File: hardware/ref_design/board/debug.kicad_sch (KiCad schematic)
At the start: 7 parts, among them J5 SWD, J6 UART, J7 DEBUG PADS, SW18 BOOTSEL, SW19 RESET

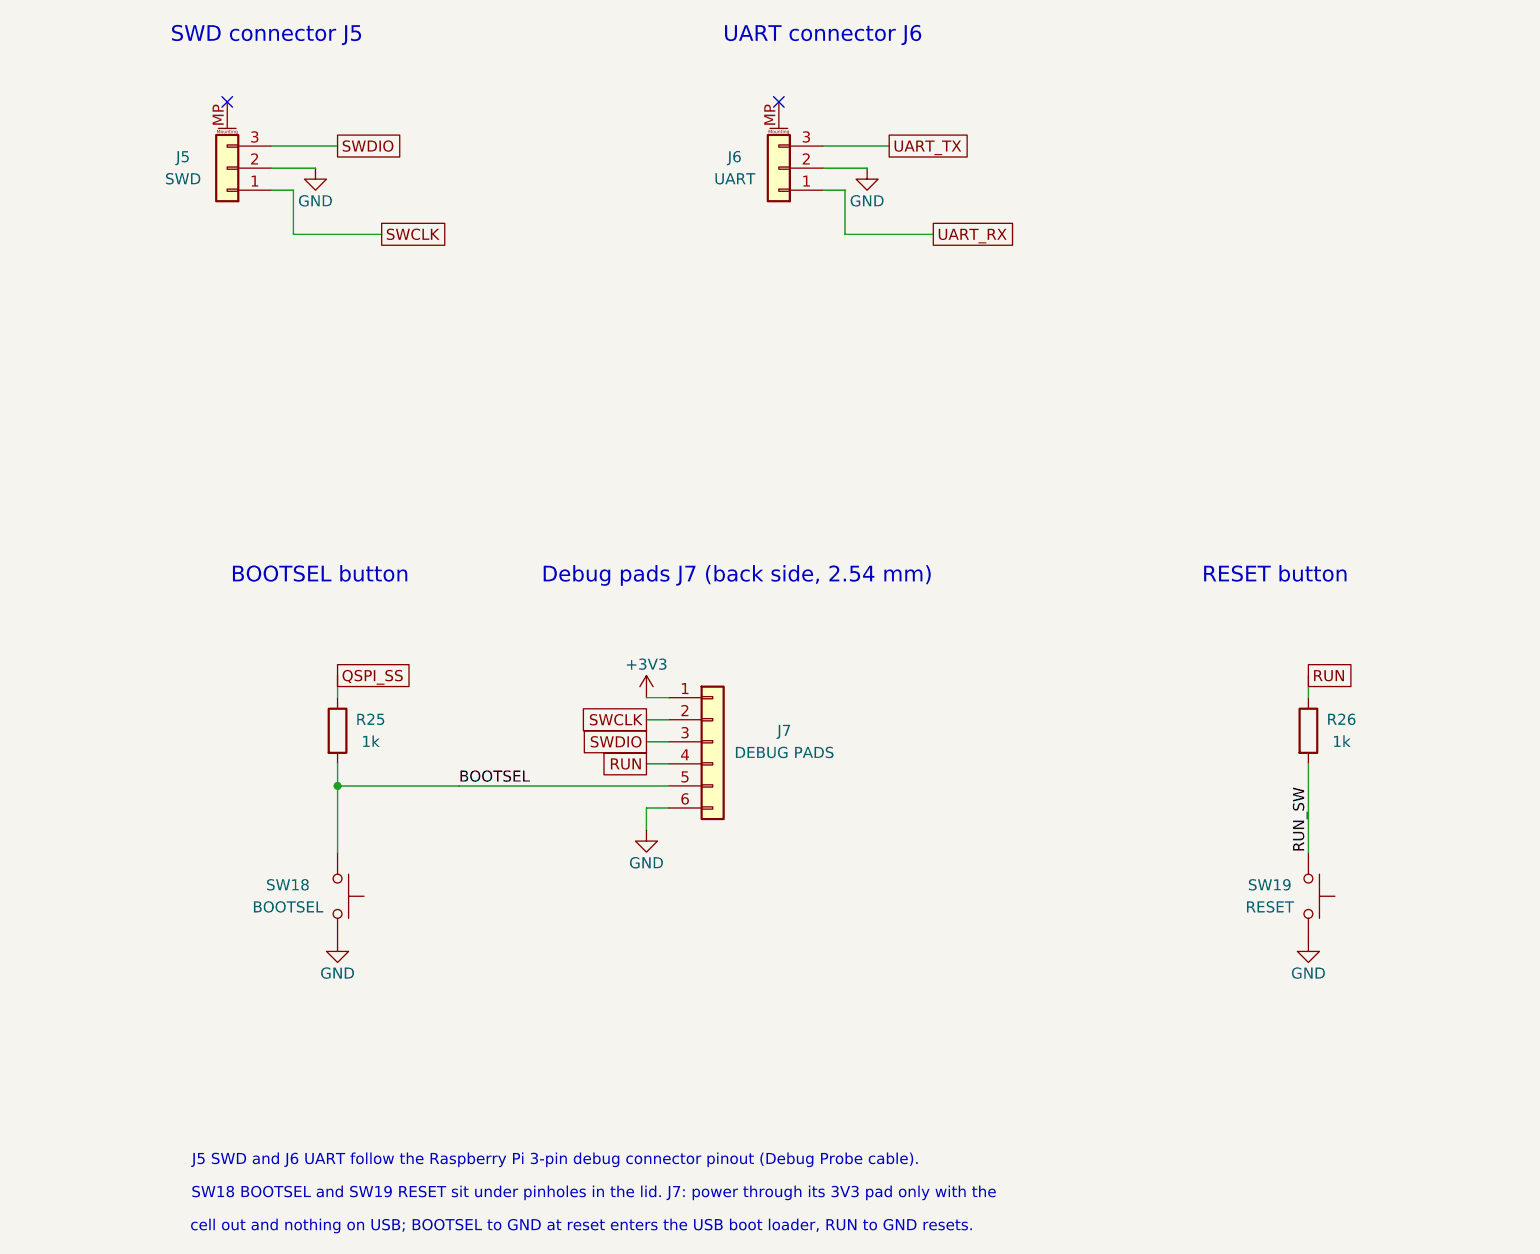
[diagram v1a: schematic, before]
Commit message: ref_design levers: pins facing their nets, no REV straps, no UART, debug buttons and latch parts out of the strips
An experiment for Alex (not on ref-design-cellcut): make the board easier to route without
changing its size.
1. GPIOs: AUDIO_PWM 8 -> 31 (PWM7 B), AMP_EN 11 -> 34, BL_PWM 44 -> 28 (PWM6 A), PWR_HOLD
   2 -> 44, P2_START 34 -> 2, P2_SELECT 9 -> 4, SR_PL 28 -> 19 (datasheet Table 3 checked;
   U4's pin review updated)
2. REV0-REV3 and R48-R51 removed (the revision stays on the silkscreen)
3. J6 (UART) and C41 removed; SW18/SW19 out of the left strip into the left bezel below H4
   (U3 and its caps 2 mm down, JP1 below the core)
4. The latch's strip parts (Q1, R16, R15, C47, TP6, D8, Q7, R62, R63) up past the hole's
   top edge under seat 2's deck; C42 to the right bezel
tools/strip_load.py counts nets through each strip: 11/15 -> 8/11, parts 8/16 -> 3/5.
Routed clean on the first finished attempt (seed 3, 4.2 min); check_pcb and check_fit pass.

Co-Authored-By: Claude Opus 5.5 <noreply@anthropic.com>
Claude-Session: https://claude.ai/code/session_01Y3mFMxLYqNeyyedvbYuRwX
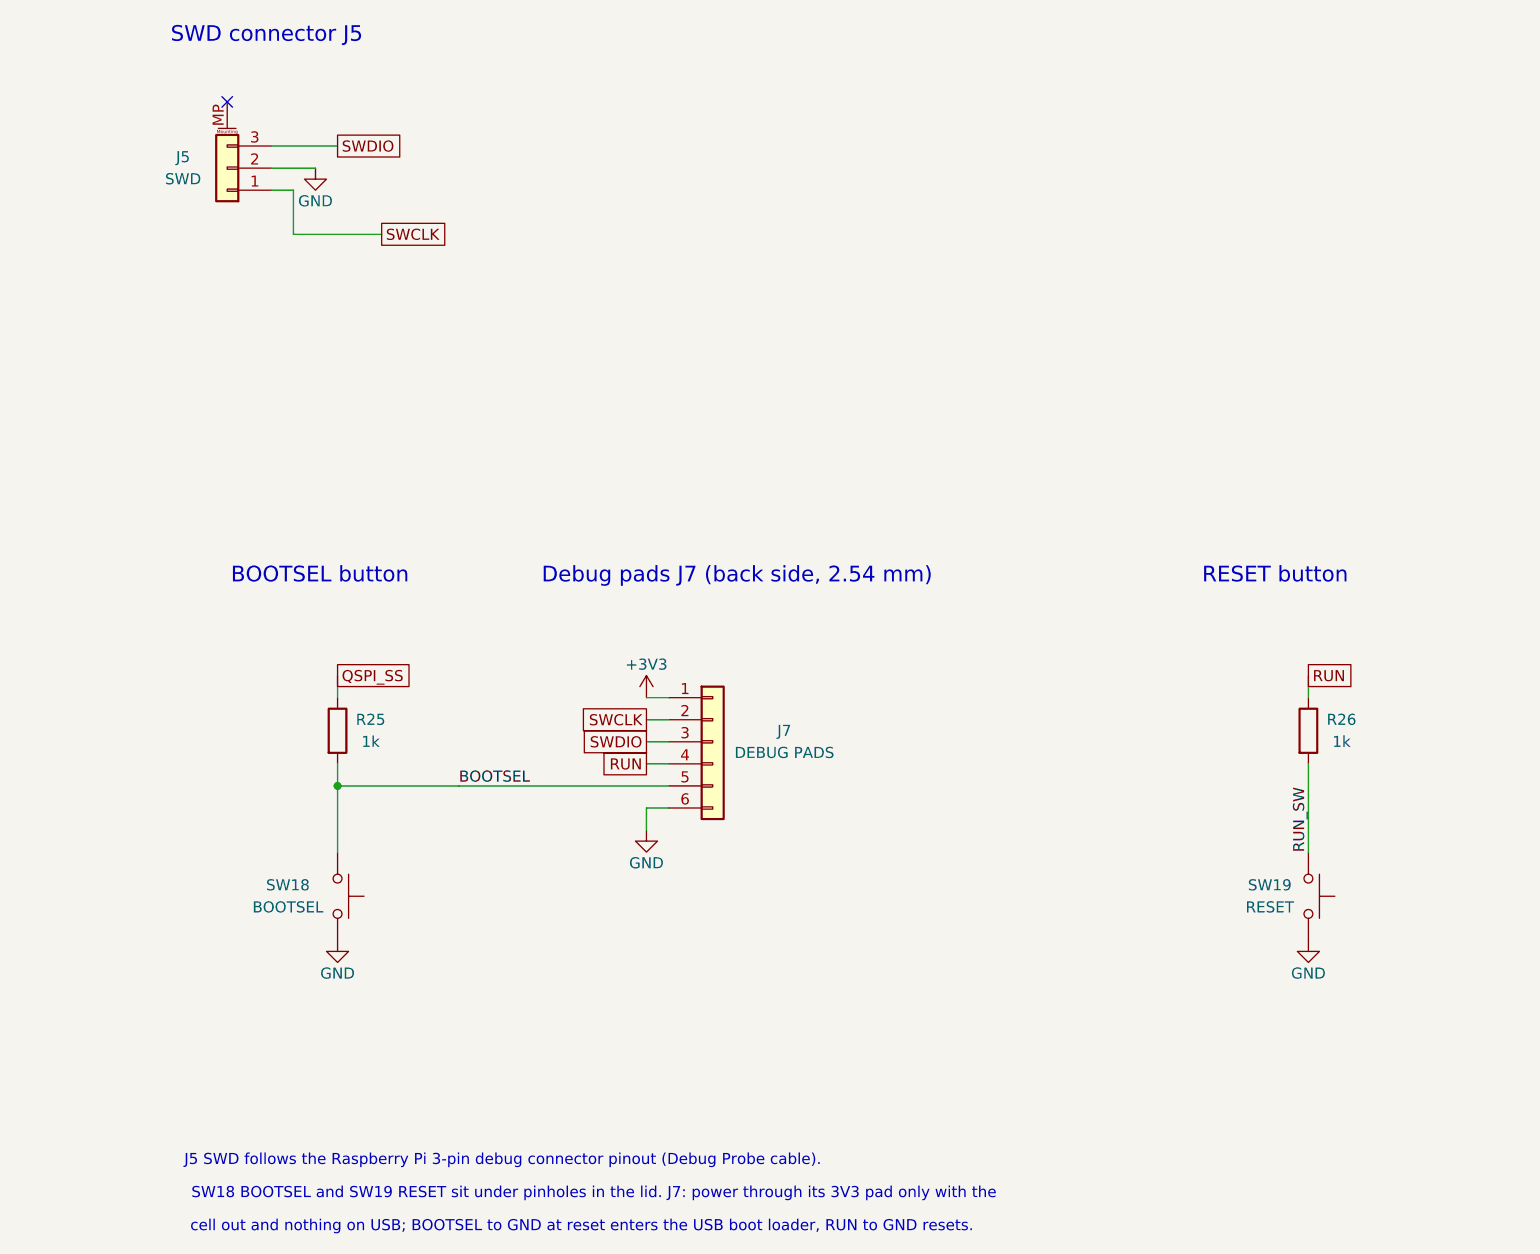
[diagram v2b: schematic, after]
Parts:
- removed J6: UART, battler:JST_SH_SM03B-SRSS-TB_1x03-1MP_P1.00mm_Horizontal, symbol Connector_Generic_MountingPin:Conn_01x03_MountingPin
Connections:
- no-connect marks 2 -> 1
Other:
- note added: "J5 SWD follows the Raspberry Pi 3-pin debug connector pinout (Debug Probe cable)."
- note removed: "J5 SWD and J6 UART follow the Raspberry Pi 3-pin debug connector pinout (Debug Probe cable)."
- note removed: "UART connector J6"
- title: SWD, UART, debug pads, BOOTSEL and RESET -> SWD, debug pads, BOOTSEL and RESET

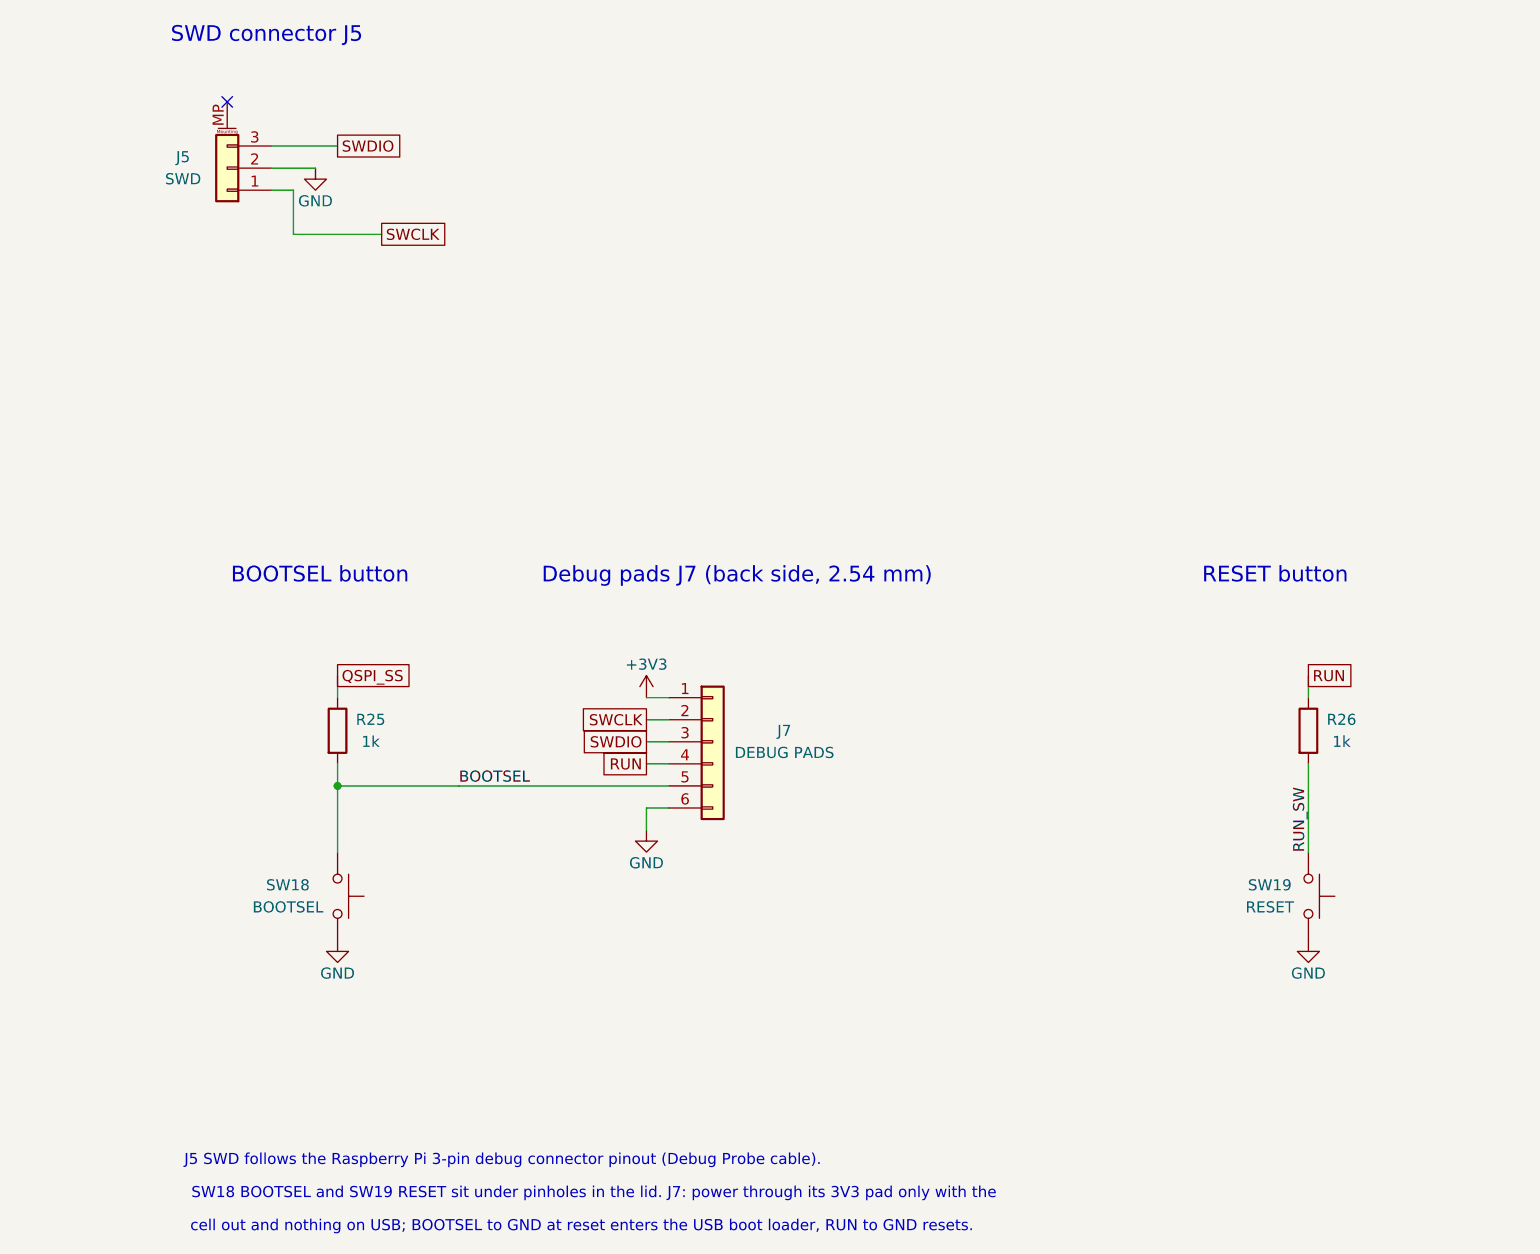
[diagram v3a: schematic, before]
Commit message: ref_design ESP32-S3 schematic: WROOM-1U-N16R8 module, TLV75733P, 8-bit 8080 panel bus (R70-R78), microSD sheet, third 74HC165, BOOT/RESET and J7 pads, 1.5k audio filter; ERC 0, netlist and pin reviews pass
Footprints: battler:ESP32-S3-WROOM-1U (KiCad's without the 0.2 mm thermal vias, tools/fp_esp32.py) and the 4-pad J7. docs/esp32s3_pinmap_diff.md lists the differences from the proposal (no GPIO differs). Unverified: JLC Basic/Extended and stock of the new parts, the DM3AT card-detect pin order.

Co-Authored-By: Claude Sonnet 5.5 <noreply@anthropic.com>
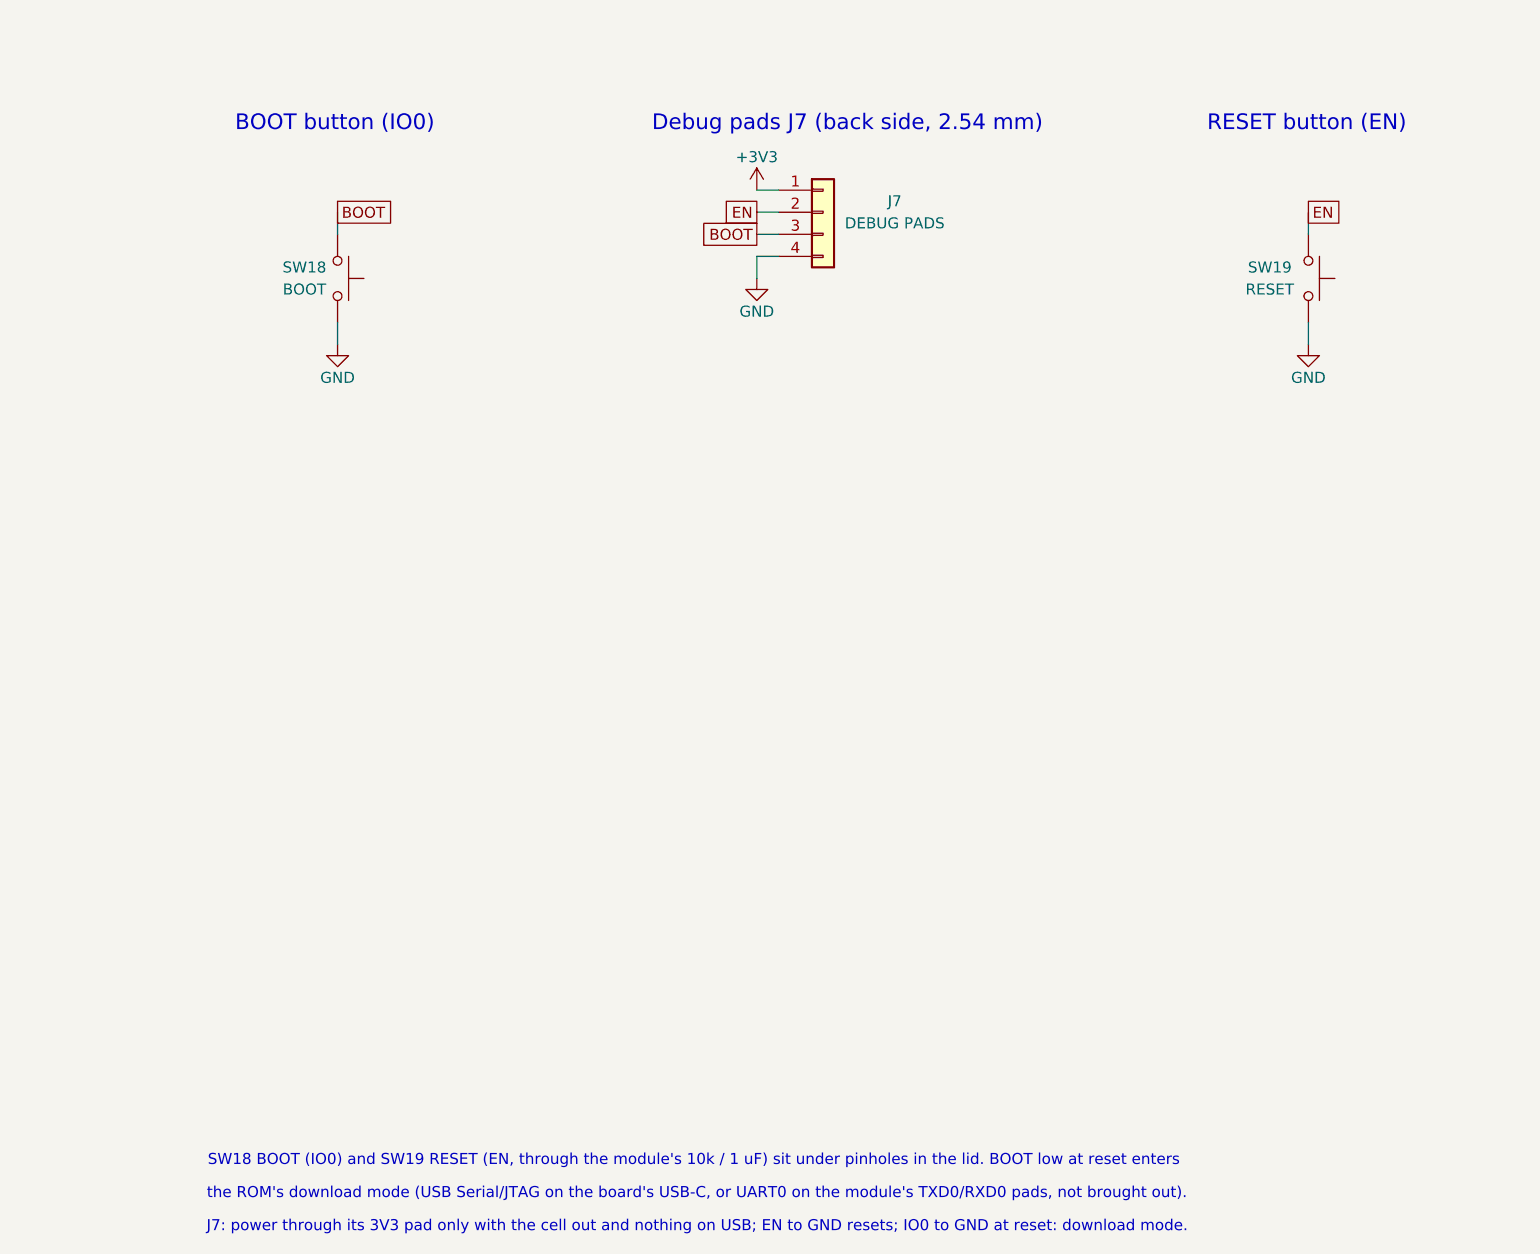
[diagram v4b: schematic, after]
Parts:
- removed J5: SWD, battler:JST_SH_SM03B-SRSS-TB_1x03-1MP_P1.00mm_Horizontal, symbol Connector_Generic_MountingPin:Conn_01x03_MountingPin
- removed R25: 1k, battler:R_0402_1005Metric_RPi, symbol Device:R
- removed R26: 1k, Resistor_SMD:R_0402_1005Metric, symbol Device:R
- J7: footprint battler:Pogo_Pads_1x06_P2.54mm -> battler:Pogo_Pads_1x04_P2.54mm; symbol Connector_Generic:Conn_01x06 -> Connector_Generic:Conn_01x04
- SW18: value BOOTSEL -> BOOT
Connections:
- net RUN is gone; now on net GND: J7.4 (Pin_4)
- net SWCLK is gone; now on net EN: J7.2 (Pin_2)
- net SWDIO is gone; now on net BOOT: J7.3 (Pin_3)
- net GND: no longer J7.6 (Pin_6)
- net BOOTSEL renamed BOOT
- net BOOT: no longer J7.5 (Pin_5)
- net RUN_SW renamed EN
- no-connect marks 1 -> 0
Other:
- note added: "BOOT button (IO0)"
- note added: "J7: power through its 3V3 pad only with the cell out and nothing on USB; EN to GND resets; IO0 to GND at reset: download mode."
- note added: "RESET button (EN)"
- note added: "SW18 BOOT (IO0) and SW19 RESET (EN, through the module's 10k / 1 uF) sit under pinholes in the lid. BOOT low at reset enters"
- note added: "the ROM's download mode (USB Serial/JTAG on the board's USB-C, or UART0 on the module's TXD0/RXD0 pads, not brought out)."
- note removed: "BOOTSEL button"
- note removed: "J5 SWD follows the Raspberry Pi 3-pin debug connector pinout (Debug Probe cable)."
- note removed: "RESET button"
- note removed: "SW18 BOOTSEL and SW19 RESET sit under pinholes in the lid. J7: power through its 3V3 pad only with the"
- note removed: "SWD connector J5"
- note removed: "cell out and nothing on USB; BOOTSEL to GND at reset enters the USB boot loader, RUN to GND resets."
- title: SWD, debug pads, BOOTSEL and RESET -> BOOT and RESET, debug pads
- moved on the sheet: SW18, SW19
